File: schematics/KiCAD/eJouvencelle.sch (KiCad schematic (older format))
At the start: 44 parts

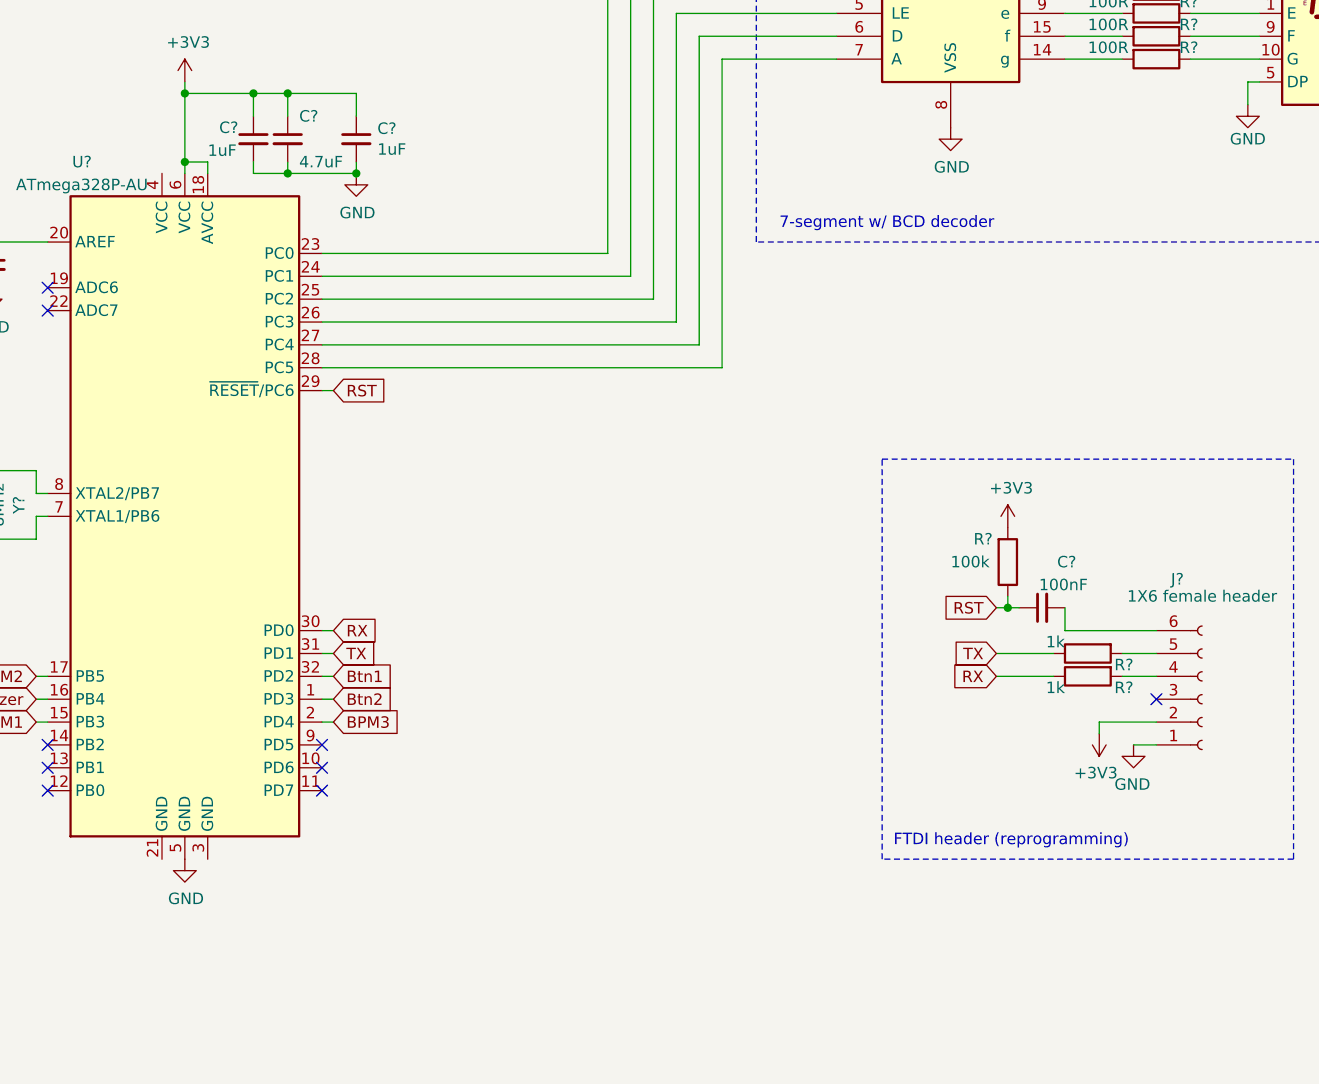
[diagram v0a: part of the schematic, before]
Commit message: fix FTDI wiring + update atmega model
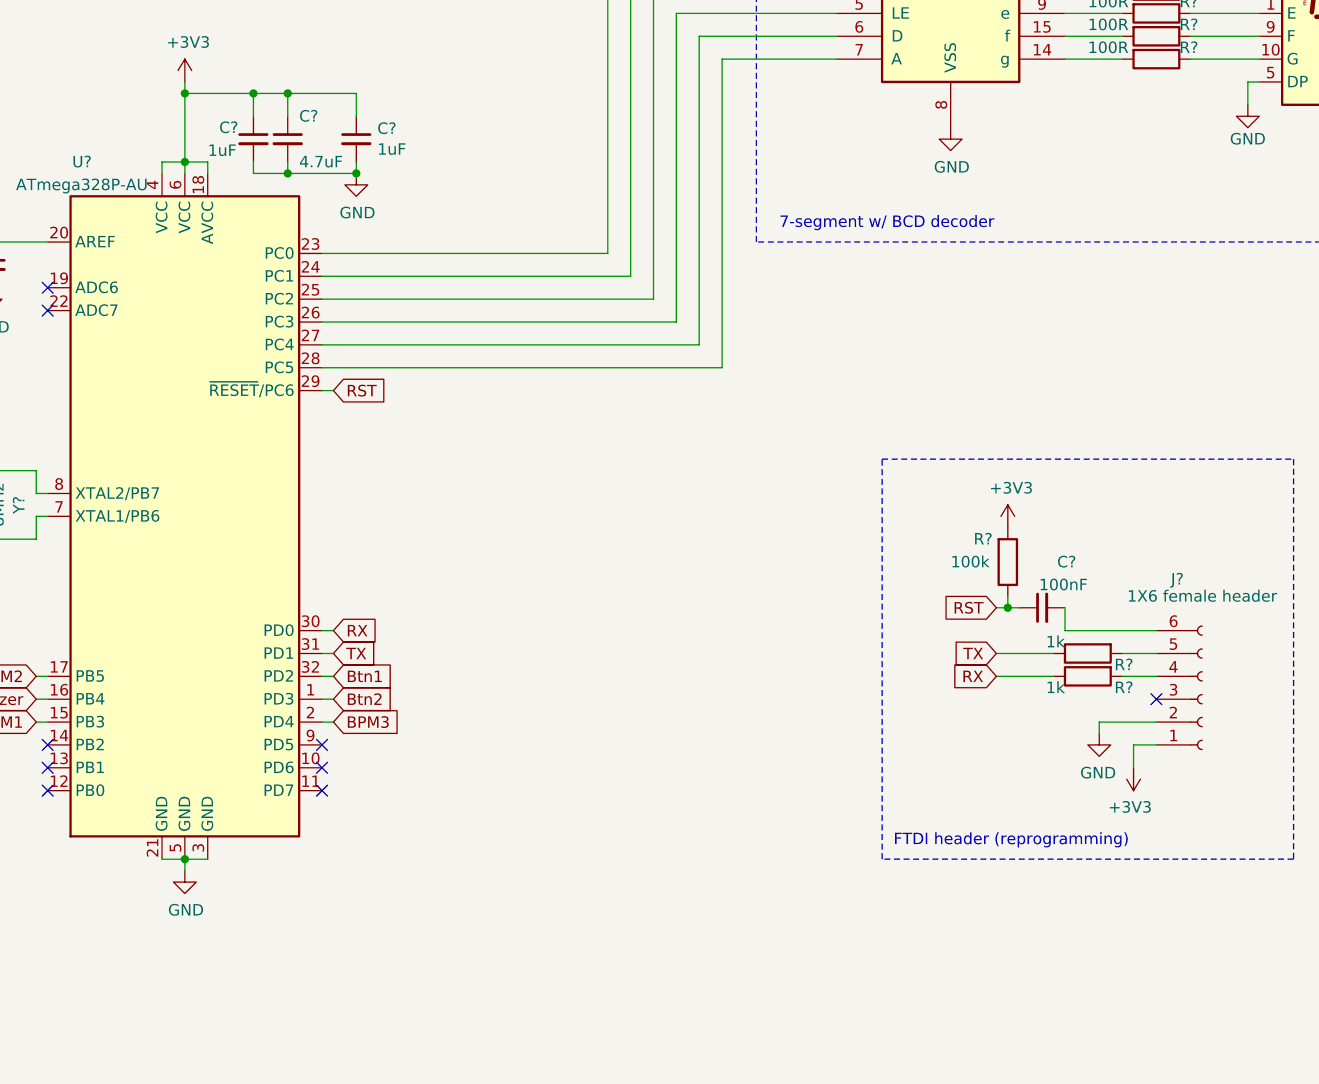
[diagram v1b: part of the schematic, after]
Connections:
- net +3V3: now also J?.1 (Pin_1), U?.4 (VCC); no longer J?.2 (Pin_2)
- net GND: now also J?.2 (Pin_2), U?.21 (GND), U?.3 (GND); no longer J?.1 (Pin_1)
